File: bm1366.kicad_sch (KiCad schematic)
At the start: 7 parts, among them J2 Conn_01x06, U35 TXU0304PW, U8 25MHz

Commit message: Refactored buck stage and improved EMI performance
I've made several changes that I’d like to explain. Not sure yet if all of them are optimal, but they reflect my impressions and should help in several areas.

- Increased buck converter from 4 to 6 phases (now using TPS53667 controller).
- Changed layer stack to keep GND between VDD planes (to improve EMI).
- Added EMI filters at input, power beads, and additional ferrite beads in the 3V3 and 5V sections.
- Relocated the 5V LDO to optimize space in the regulator area.
- Standardized some input capacitors in the buck regulator stage.
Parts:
- C25, C82, C83: LCSC (none) -> C519981
- R8: LCSC (none) -> C140868
- U35: LCSC (none) -> C4364118
- U8: LCSC (none) -> C5137262
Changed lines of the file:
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@@
+			)
+		)
+		(property "LCSC" "C4364118"
+			(at 147.32 36.83 0)
+			(effects
+				(font
+					(size 1.27 1.27)
+				)
+				(hide yes)
 			)
 		)
@@
 			)
 		)
+		(property "LCSC" "C519981"
+			(at 115.57 35.56 0)
+			(effects
+				(font
+					(size 1.27 1.27)
+				)
+				(hide yes)
+			)
+		)
 		(pin "1"
 		)
@@
 		(property "OrderNr" "311-3037-1-ND"
 			(at 30.48 90.17 0)
+			(effects
+				(font
+					(size 1.27 1.27)
+				)
+				(hide yes)
+			)
+		)
+		(property "LCSC" "C519981"
+			(at 30.48 90.17 90)
 			(effects
 				(font
@@
 			)
 		)
+		(property "LCSC" "C5137262"
+			(at 49.53 85.09 0)
+			(effects
+				(font
+					(size 1.27 1.27)
+				)
+				(hide yes)
+			)
+		)
 		(pin "1"
 		)
@@
 			)
 		)
+		(property "LCSC" "C140868"
+			(at 71.12 106.68 90)
+			(effects
+				(font
+					(size 1.27 1.27)
+				)
+				(hide yes)
+			)
+		)
 		(pin "1"
 		)
@@
 			(at 109.22 35.56 0)
 			(effects
+				(font
+					(size 1.27 1.27)
+				)
+				(hide yes)
+			)
+		)
+		(property "LCSC" "C519981"
+			(at 109.22 35.56 0)
+			(effects

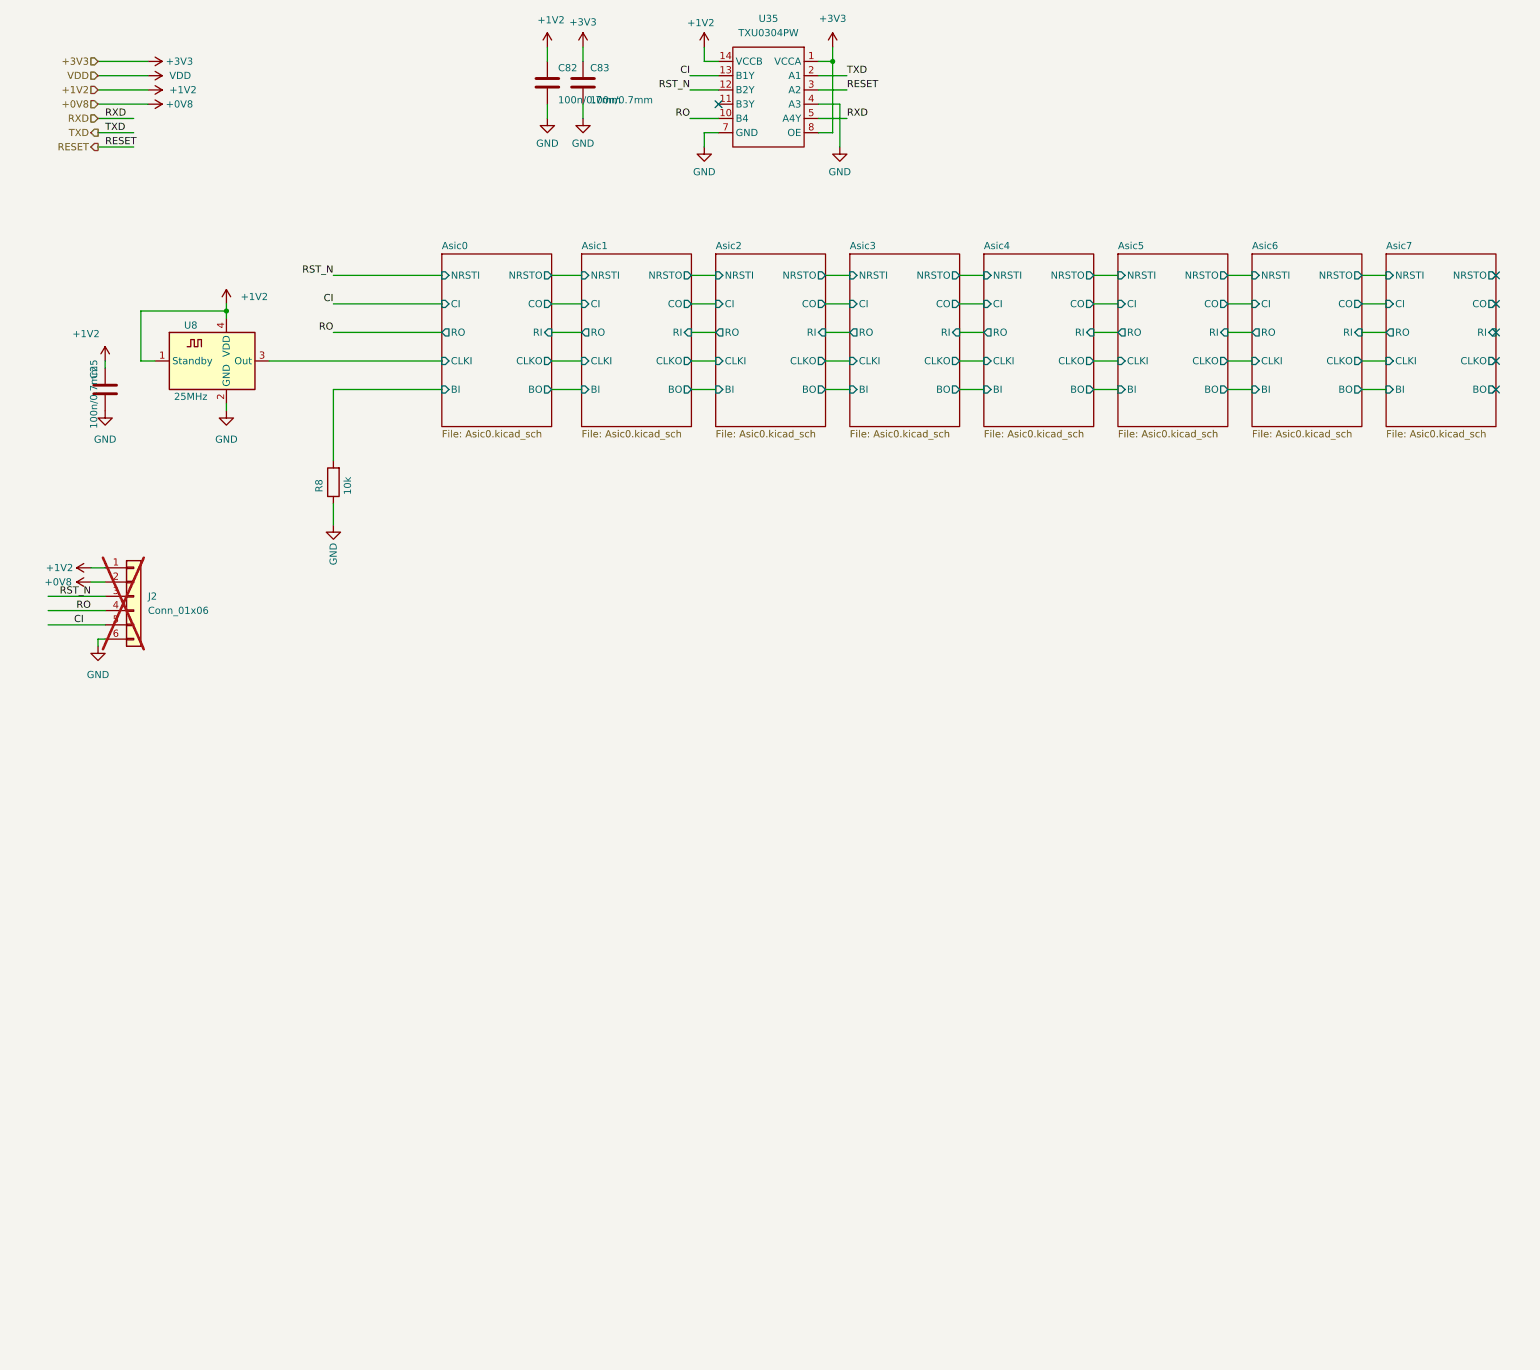
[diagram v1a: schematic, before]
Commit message: Added TMP451 to schematic
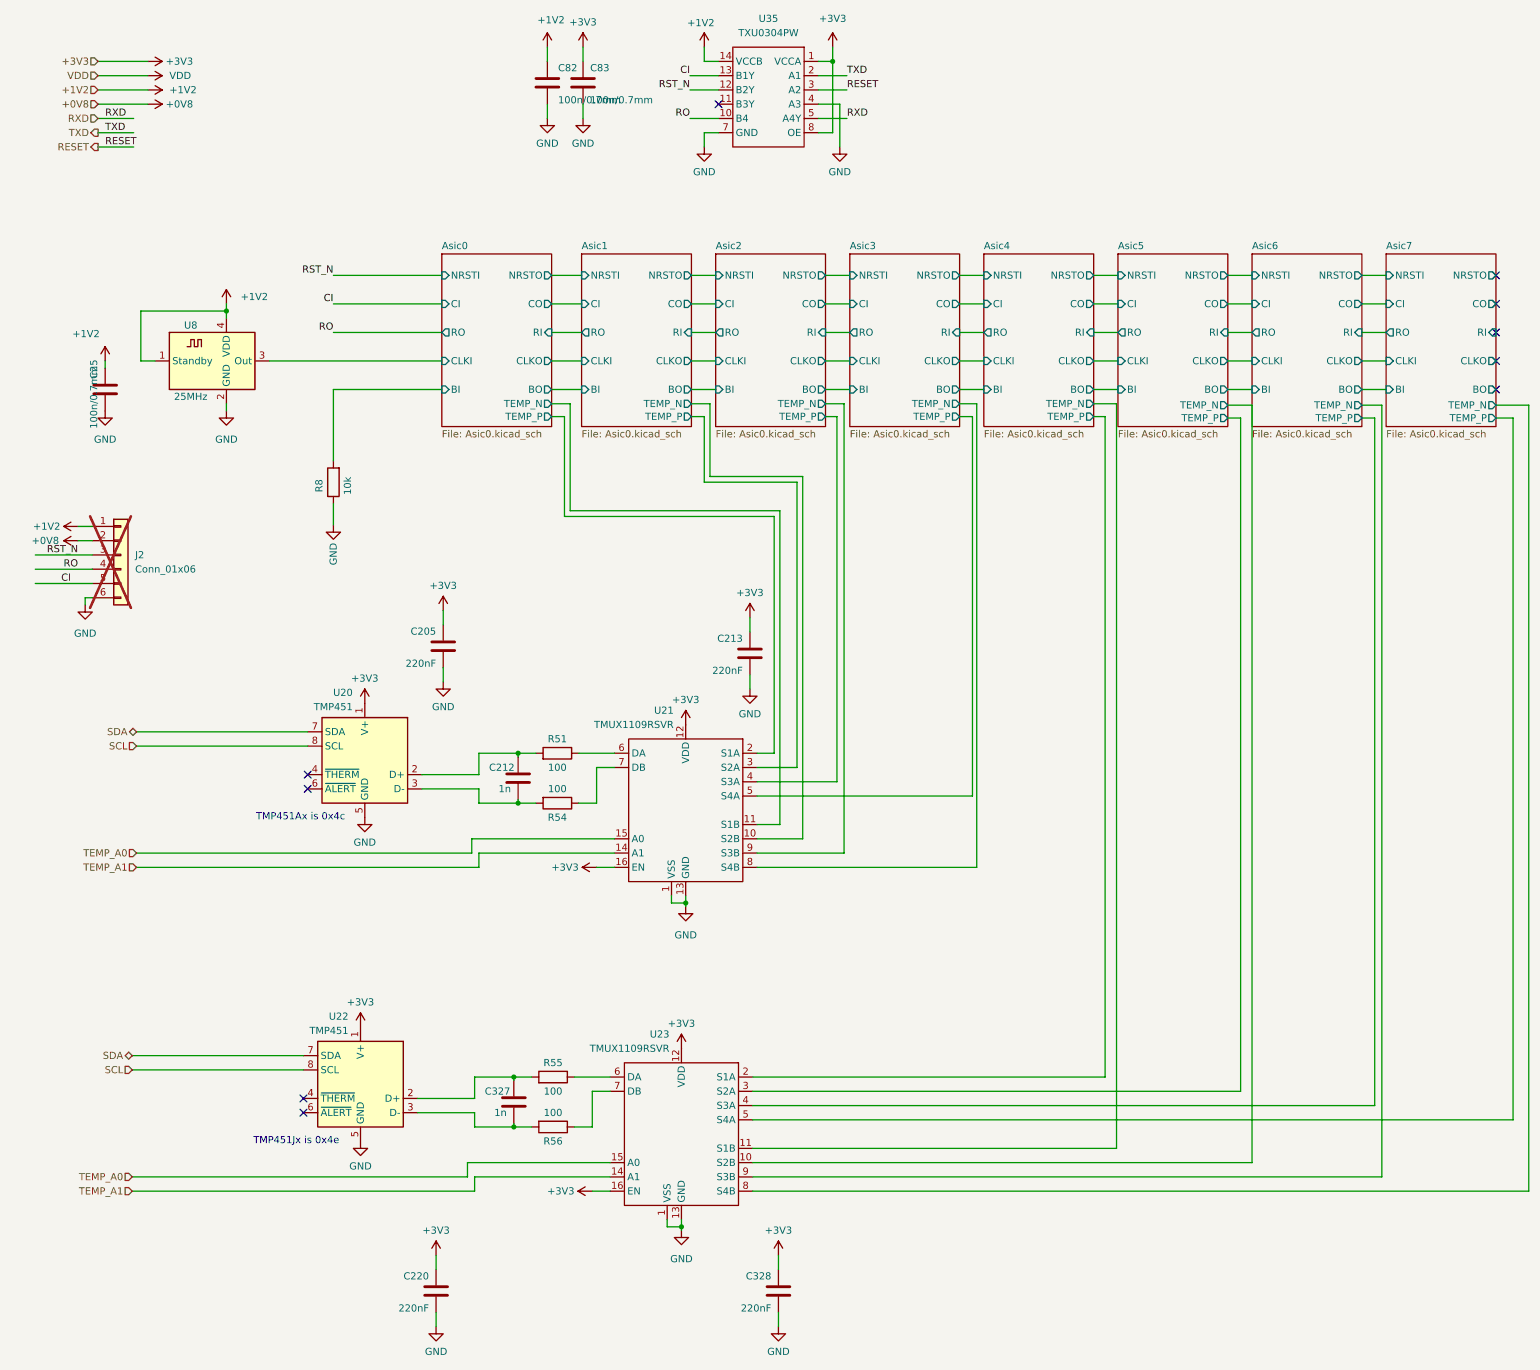
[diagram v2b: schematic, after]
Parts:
- added C205, C213, C220, C328: 220nF, Capacitor_SMD:C_0805_2012Metric, symbol Device:C
- added C212, C327: 1n, Capacitor_SMD:C_0805_2012Metric, symbol Device:C
- added R51, R54, R55, R56: 100, Resistor_SMD:R_0805_2012Metric, symbol Device:R
- added U20, U22: TMP451, Package_SON:WSON-8-1EP_2x2mm_P0.5mm_EP0.9x1.6mm, symbol Sensor_Temperature:TMP411
- added U21, U23: TMUX1109RSVR, Package_DFN_QFN:UQFN-16_1.8x2.6mm_P0.4mm, symbol mylib7:TMUX1109
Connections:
- net +3V3: now also C205.1, C213.1, C220.1, C328.1, U20.1 (V+), U21.12 (VDD), U21.16 (EN), U22.1 (V+), U23.12 (VDD), U23.16 (EN)
- net GND: now also C205.2, C213.2, C220.2, C328.2, U20.5 (GND), U21.1 (VSS), U21.13 (GND), U22.5 (GND), U23.1 (VSS), U23.13 (GND)
- new net: R51.1, U21.6 (DA)
- new net: R54.1, U21.7 (DB)
- new net: R55.1, U23.6 (DA)
- new net: R56.1, U23.7 (DB)
- new net: C212.1, R51.2, U20.2 (D+)
- new net: C212.2, R54.2, U20.3 (D-)
- new net: C327.1, R55.2, U22.2 (D+)
- new net: C327.2, R56.2, U22.3 (D-)
- new net Asic0/TEMP_N: U21.11 (S1B)
- new net Asic0/TEMP_P: U21.2 (S1A)
- new net Asic1/TEMP_N: U21.10 (S2B)
- new net Asic1/TEMP_P: U21.3 (S2A)
- new net Asic2/TEMP_N: U21.9 (S3B)
- new net Asic2/TEMP_P: U21.4 (S3A)
- new net Asic3/TEMP_N: U21.8 (S4B)
- new net Asic3/TEMP_P: U21.5 (S4A)
- new net Asic4/TEMP_N: U23.11 (S1B)
- new net Asic4/TEMP_P: U23.2 (S1A)
- new net Asic5/TEMP_N: U23.10 (S2B)
- new net Asic5/TEMP_P: U23.3 (S2A)
- new net Asic6/TEMP_N: U23.9 (S3B)
- new net Asic6/TEMP_P: U23.4 (S3A)
- new net Asic7/TEMP_N: U23.8 (S4B)
- new net Asic7/TEMP_P: U23.5 (S4A)
- new net SCL: U20.8 (SCL), U22.8 (SCL)
- new net SDA: U20.7 (SDA), U22.7 (SDA)
- new net TEMP_A0: U21.15 (A0), U23.15 (A0)
- new net TEMP_A1: U21.14 (A1), U23.14 (A1)
- no-connect marks 6 -> 10
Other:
- sheet Asic0 ports: added TEMP_N, TEMP_P; removed none
- sheet Asic1 ports: added TEMP_N, TEMP_P; removed none
- sheet Asic2 ports: added TEMP_N, TEMP_P; removed none
- sheet Asic3 ports: added TEMP_N, TEMP_P; removed none
- sheet Asic4 ports: added TEMP_N, TEMP_P; removed none
- sheet Asic5 ports: added TEMP_N, TEMP_P; removed none
- sheet Asic6 ports: added TEMP_N, TEMP_P; removed none
- sheet Asic7 ports: added TEMP_N, TEMP_P; removed none
- note added: "TMP451Ax is 0x4c"
- note added: "TMP451Jx is 0x4e"
- moved on the sheet: J2

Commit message: PCB w Tempmeasurement
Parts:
- U20: value TMP451 -> TMP451A
- U22: value TMP451 -> TMP451J
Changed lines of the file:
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@@
 	(wire
 		(pts
-			(xy 66.548 153.67) (xy 36.068 153.67)
+			(xy 66.548 153.67) (xy 19.812 153.67)
 		)
 		(stroke
@@
 	(wire
 		(pts
-			(xy 66.548 151.13) (xy 36.068 151.13)
+			(xy 19.812 151.13) (xy 66.548 151.13)
 		)
 		(stroke
@@
 		)
 	)
-	(hierarchical_label "SCL"
-		(shape input)
-		(at 36.068 153.67 180)
+	(hierarchical_label "SDA"
+		(shape bidirectional)
+		(at 35.306 208.788 180)
 		(effects
 			(font
@@
 		)
 	)
-	(hierarchical_label "SDA"
-		(shape bidirectional)
-		(at 36.068 151.13 180)
+	(hierarchical_label "SCL"
+		(shape input)
+		(at 19.812 153.67 180)
 		(effects
 			(font
@@
 		)
 	)
-	(hierarchical_label "RXD"
-		(shape input)
-		(at 29.21 41.91 180)
+	(hierarchical_label "SDA"
+		(shape bidirectional)
+		(at 19.812 151.13 180)
 		(effects
 			(font
@@
 		)
 	)
-	(hierarchical_label "SDA"
-		(shape bidirectional)
-		(at 35.306 208.788 180)
+	(hierarchical_label "RXD"
+		(shape input)
+		(at 29.21 41.91 180)
 		(effects
 			(font
@@
 		(fields_autoplaced yes)
 		(property "Reference" "U20"
-			(at 74.5647 144.145 0)
+			(at 79.8261 143.51 0)
 			(effects
 				(font
 					(size 1.27 1.27)
 				)
-				(justify left)
+				(justify right)
 			)
 		)
-		(property "Value" "TMP451"
-			(at 74.5647 146.685 0)
+		(property "Value" "TMP451A"
+			(at 79.8261 146.05 0)
 			(effects
 				(font
 					(size 1.27 1.27)
 				)
-				(justify left)
+				(justify right)
 			)
 		)
@@
 		(fields_autoplaced yes)
 		(property "Reference" "U22"
-			(at 73.8027 201.803 0)
+			(at 79.0641 200.66 0)
 			(effects
 				(font
 					(size 1.27 1.27)
 				)
-				(justify left)
+				(justify right)
 			)
 		)
-		(property "Value" "TMP451"
-			(at 73.8027 204.343 0)
+		(property "Value" "TMP451J"
+			(at 79.0641 203.2 0)
 			(effects
 				(font
 					(size 1.27 1.27)
 				)
-				(justify left)
+				(justify right)
 			)
 		)

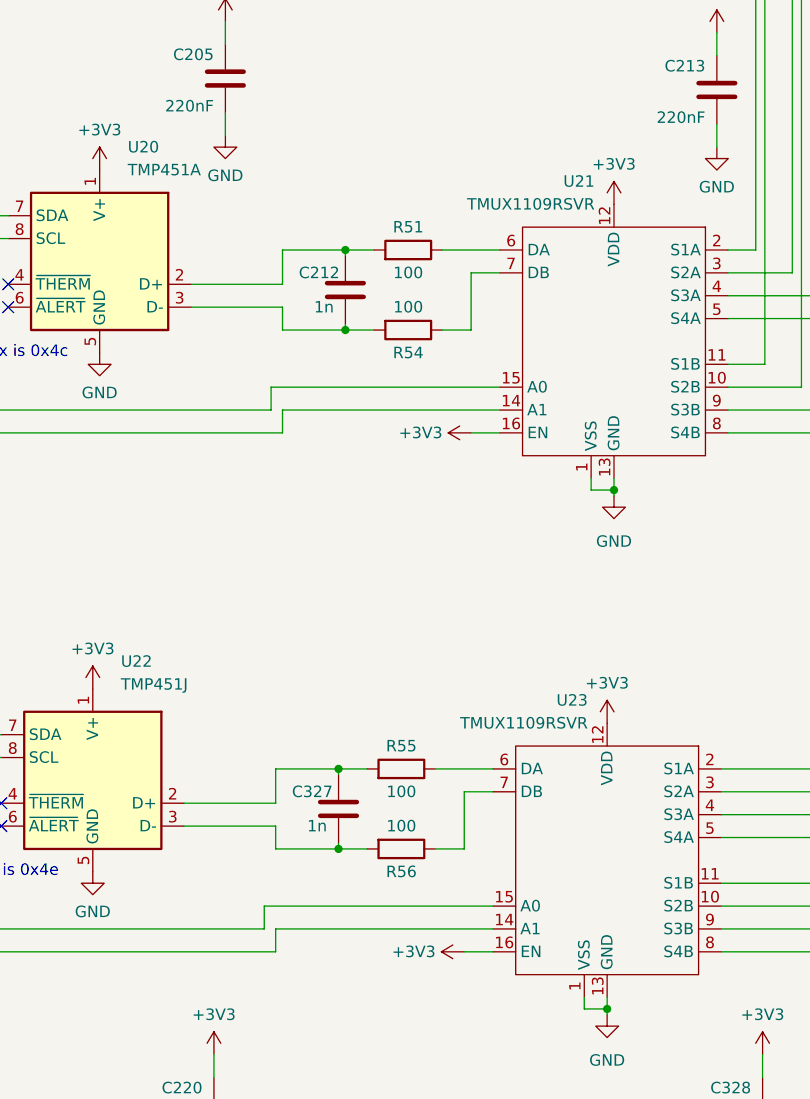
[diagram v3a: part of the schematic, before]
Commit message: Corrected Partnumbers (DK)
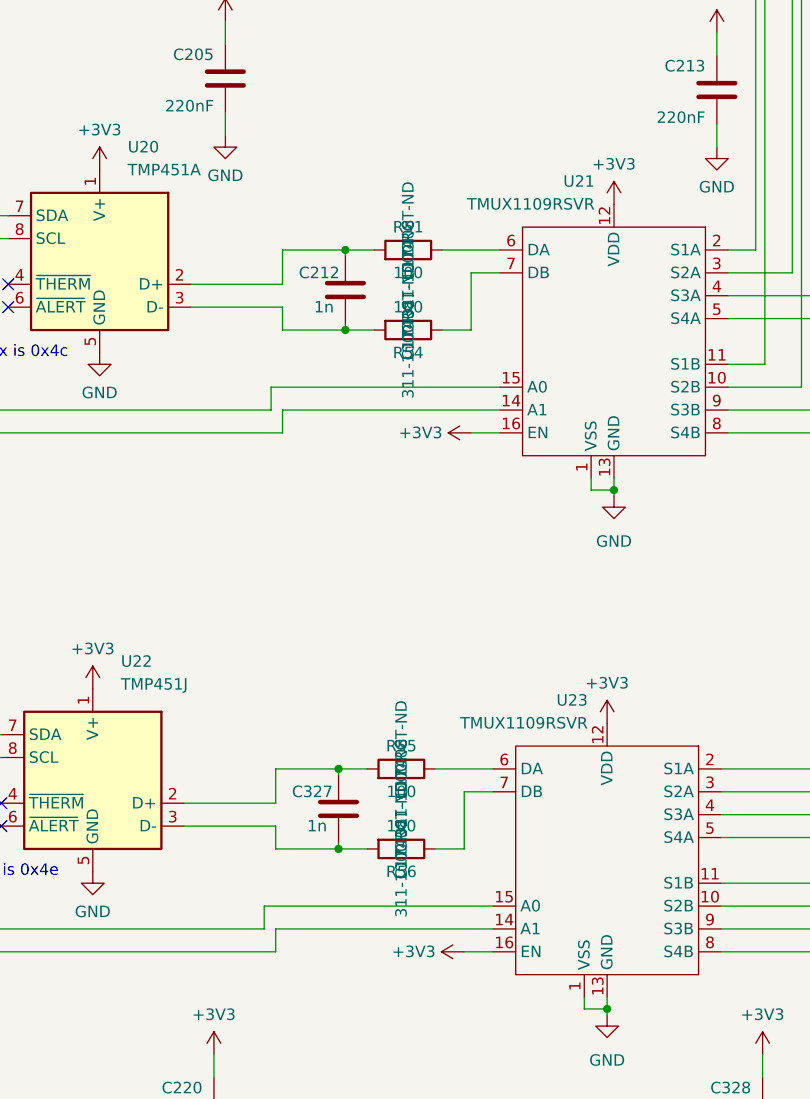
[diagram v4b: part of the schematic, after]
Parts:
- C205, C212, C213, C220, C327, C328: Distributor Digikey -> D
- R51, R54, R55, R56: Distributor (none) -> D; LCSC (none) -> C17408; OrderNr (none) -> 311-100CRCT-ND
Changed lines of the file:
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@@
 			)
 		)
-		(property "Distributor" "Digikey"
+		(property "Distributor" "D"
 			(at 89.408 250.698 0)
 			(effects
@@
 			)
 		)
+		(property "Distributor" "D"
+			(at 110.998 163.83 0)
+			(effects
+				(font
+					(size 1.27 1.27)
+				)
+			)
+		)
+		(property "LCSC" "C17408"
+			(at 110.998 163.83 0)
+			(effects
+				(font
+					(size 1.27 1.27)
+				)
+			)
+		)
+		(property "OrderNr" "311-100CRCT-ND"
+			(at 110.998 163.83 0)
+			(effects
+				(font
+					(size 1.27 1.27)
+				)
+			)
+		)
 		(pin "1"
 		)
@@
 			)
 		)
-		(property "Distributor" "Digikey"
+		(property "Distributor" "D"
 			(at 145.288 137.16 0)
 			(effects
@@
 			)
 		)
+		(property "Distributor" "D"
+			(at 110.236 212.598 0)
+			(effects
+				(font
+					(size 1.27 1.27)
+				)
+			)
+		)
+		(property "LCSC" "C17408"
+			(at 110.236 212.598 0)
+			(effects
+				(font
+					(size 1.27 1.27)
+				)
+			)
+		)
+		(property "OrderNr" "311-100CRCT-ND"
+			(at 110.236 212.598 0)
+			(effects
+				(font
+					(size 1.27 1.27)
+				)
+			)
+		)
 		(pin "1"
 		)
@@
 			)
 		)
-		(property "Distributor" "Digikey"
+		(property "Distributor" "D"
 			(at 150.368 250.698 0)
 			(effects
@@
 			)
 		)
-		(property "Distributor" "Digikey"
+		(property "Distributor" "D"
 			(at 90.678 135.89 0)
 			(effects
@@
 			)
 		)
+		(property "Distributor" "D"
+			(at 110.998 154.94 0)
+			(effects
+				(font
+					(size 1.27 1.27)
+				)
+			)
+		)
+		(property "LCSC" "C17408"
+			(at 110.998 154.94 0)
+			(effects
+				(font
+					(size 1.27 1.27)
+				)
+			)
+		)
+		(property "OrderNr" "311-100CRCT-ND"
+			(at 110.998 154.94 0)
+			(effects
+				(font
+					(size 1.27 1.27)
+				)
+			)
+		)
 		(pin "1"
 		)
@@
 			)
 		)
+		(property "Distributor" "D"
+			(at 110.236 221.488 0)
+			(effects
+				(font
+					(size 1.27 1.27)
+				)
+			)
+		)
+		(property "LCSC" "C17408"
+			(at 110.236 221.488 0)
+			(effects
+				(font
+					(size 1.27 1.27)
+				)
+			)
+		)
+		(property "OrderNr" "311-100CRCT-ND"
+			(at 110.236 221.488 0)
+			(effects
+				(font
+					(size 1.27 1.27)
+				)
+			)
+		)
 		(pin "1"
 		)
@@
 			)
 		)
-		(property "Distributor" "Digikey"
+		(property "Distributor" "D"
 			(at 103.251 217.043 0)
 			(effects
@@
 			)
 		)
-		(property "Distributor" "Digikey"
+		(property "Distributor" "D"
 			(at 104.013 159.385 0)
 			(effects
